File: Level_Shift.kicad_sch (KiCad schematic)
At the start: 23 parts, among them U23 74AVC4T245, U25 74AVC4T245, U26 74LVC8T245, U27 74LVC8T245

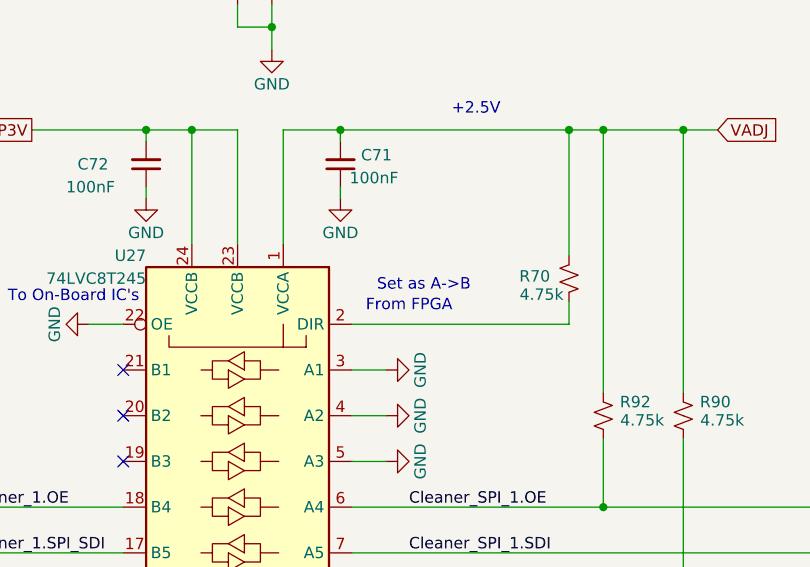
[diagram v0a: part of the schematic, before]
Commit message: Changes to Power Filtering
- Removed extra bulk caps on FMC power inputs
- Cleaned up some power routing between U22 & U44
- Made some vias larger for power tree connections
- Changed 22uF to a new 35V part
- Changed 10uF part to a new equivalent part due to OOS.
- Modified text near U27 on schematic for clarity
- Added notes on the power schematics showing effective capacitance of chosen bulk mlcc caps
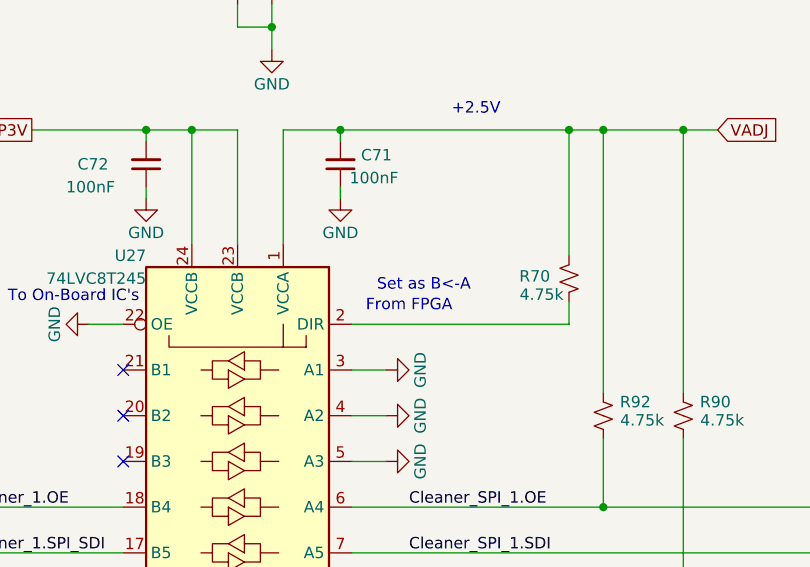
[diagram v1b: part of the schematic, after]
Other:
- note removed: "Set as A->B"
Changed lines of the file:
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@@
 		)
 	)
-	(text "Set as A->B"
+	(text "Set as B<-A\n"
 		(exclude_from_sim no)
 		(at 319.278 128.524 0)
